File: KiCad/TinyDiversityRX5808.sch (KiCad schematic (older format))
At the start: 23 parts, among them J1 Googles, J2 RX_A, J3 RX_B, J4 Conn_01x06, SW1 SW_Push, U1 MAX4624, U2 ATTINY85-20SU

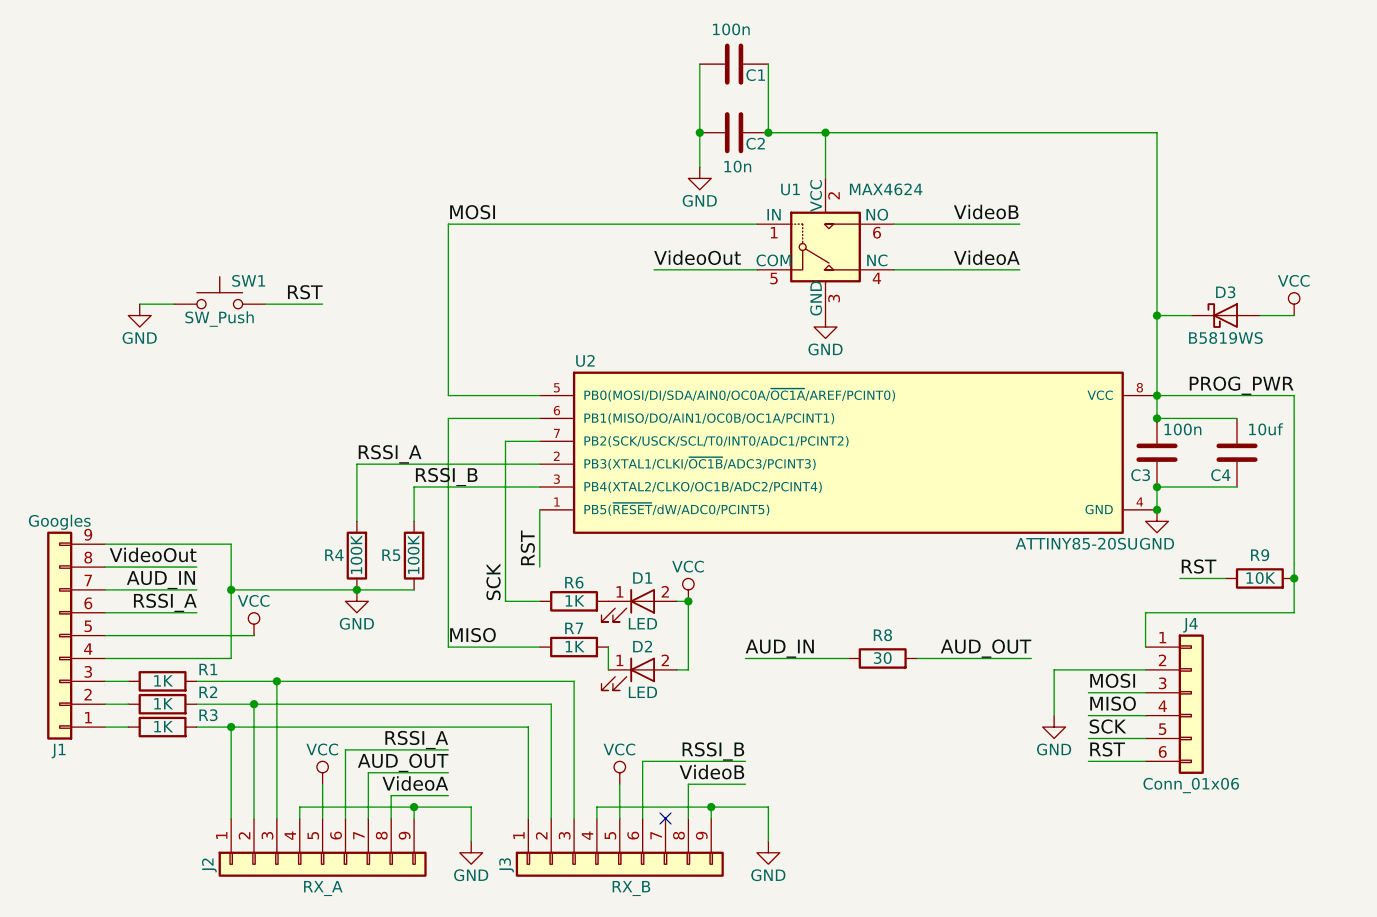
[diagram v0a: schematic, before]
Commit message: Layout change for easier solder and more thin design
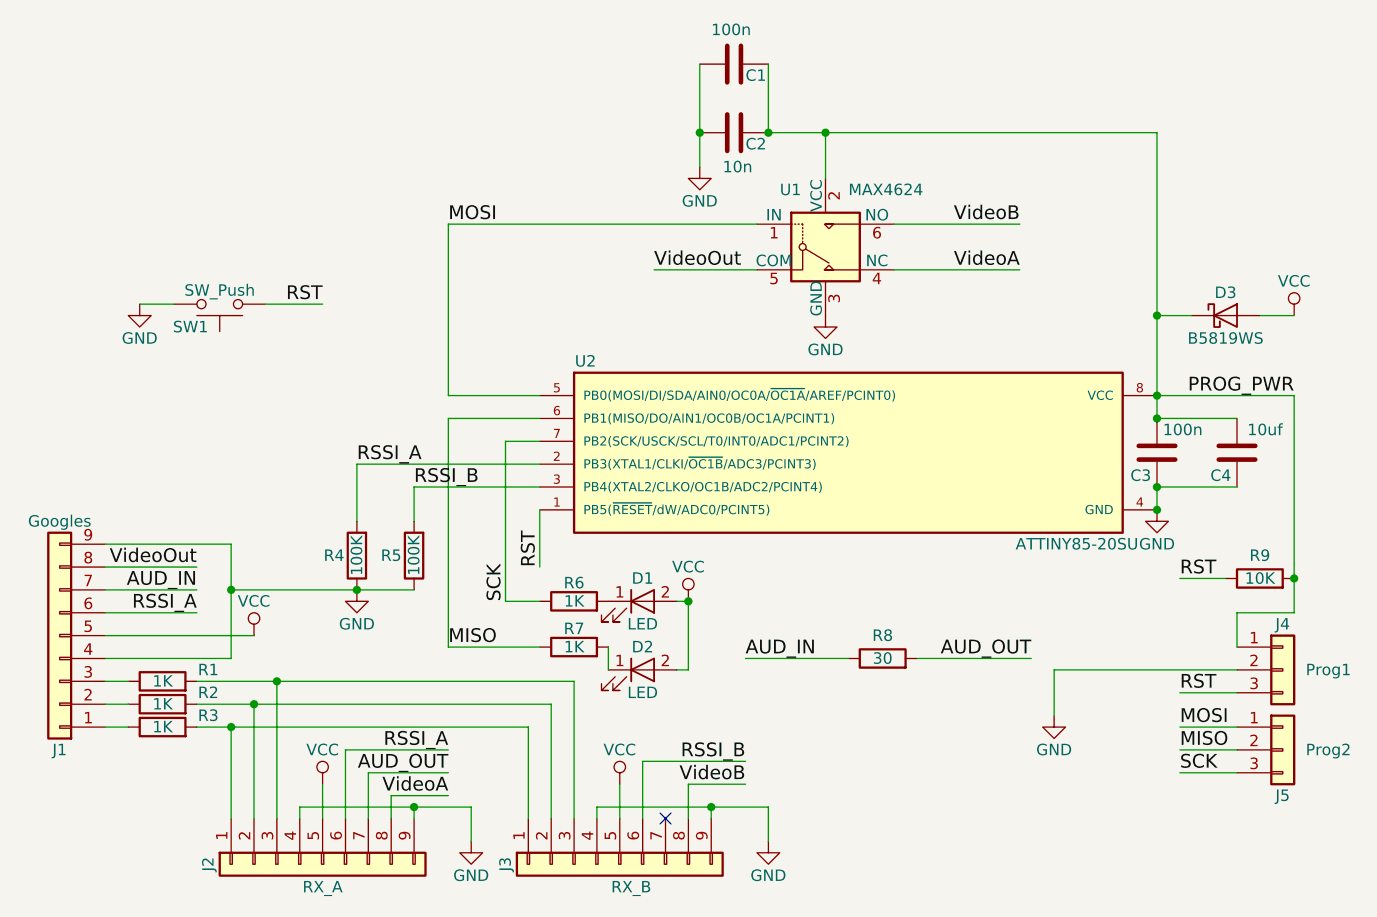
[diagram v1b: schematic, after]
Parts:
- removed J4: Conn_01x06, KiCadCustomLibs:Pads_prog_6pin1.25mm, symbol Conn_01x06
- added J4: Prog1, KiCadCustomLibs:Pads_prog_3pin1.25mm, symbol Conn_01x03
- added J5: Prog2, KiCadCustomLibs:Pads_prog_3pin1.25mm, symbol Conn_01x03
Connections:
- net GND: now also SW1.2, J4.2 (Pin_2); no longer SW1.1
- net MISO: now also J5.2 (Pin_2)
- net MOSI: now also J5.1 (Pin_1)
- net PROG_PWR: now also J4.1 (Pin_1)
- net RST: now also SW1.1, J4.3 (Pin_3); no longer SW1.2
- net SCK: now also J5.3 (Pin_3)
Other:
- moved on the sheet: SW1
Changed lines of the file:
@@
 $EndComp
 $Comp
-L GND #PWR01
+L GND #PWR10
 U 1 1 5A0C59A7
 P 5550 2850
-F 0 "#PWR01" H 5550 2600 50  0001 C CNN
+F 0 "#PWR10" H 5550 2600 50  0001 C CNN
 F 1 "GND" H 5550 2700 50  0000 C CNN
 F 2 "" H 5550 2850 50  0001 C CNN
@@
 $EndComp
 $Comp
-L GND #PWR02
+L GND #PWR12
 U 1 1 5A0C59D1
 P 7000 3700
-F 0 "#PWR02" H 7000 3450 50  0001 C CNN
+F 0 "#PWR12" H 7000 3450 50  0001 C CNN
 F 1 "GND" H 7000 3550 50  0000 C CNN
 F 2 "" H 7000 3700 50  0001 C CNN
@@
 RSSI_B
 $Comp
-L GND #PWR03
+L GND #PWR1
 U 1 1 5A0C5ED9
 P 2550 2800
-F 0 "#PWR03" H 2550 2550 50  0001 C CNN
+F 0 "#PWR1" H 2550 2550 50  0001 C CNN
 F 1 "GND" H 2550 2650 50  0000 C CNN
 F 2 "" H 2550 2800 50  0001 C CNN
@@
 $EndComp
 $Comp
-L VCC #PWR04
+L VCC #PWR13
 U 1 1 5A0C6148
 P 7600 2850
-F 0 "#PWR04" H 7600 2700 50  0001 C CNN
+F 0 "#PWR13" H 7600 2700 50  0001 C CNN
 F 1 "VCC" H 7600 3000 50  0000 C CNN
 F 2 "" H 7600 2850 50  0001 C CNN
@@
 $EndComp
 $Comp
-L VCC #PWR05
+L VCC #PWR2
 U 1 1 5A0C6355
 P 3050 4250
-F 0 "#PWR05" H 3050 4100 50  0001 C CNN
+F 0 "#PWR2" H 3050 4100 50  0001 C CNN
 F 1 "VCC" H 3050 4400 50  0000 C CNN
 F 2 "" H 3050 4250 50  0001 C CNN
@@
 $EndComp
 $Comp
-L GND #PWR06
+L GND #PWR8
 U 1 1 5A0C6978
 P 5000 2200
-F 0 "#PWR06" H 5000 1950 50  0001 C CNN
+F 0 "#PWR8" H 5000 1950 50  0001 C CNN
 F 1 "GND" H 5000 2050 50  0000 C CNN
 F 2 "" H 5000 2200 50  0001 C CNN
@@
 $EndComp
 $Comp
-L VCC #PWR07
+L VCC #PWR7
 U 1 1 5A0C6F3D
 P 4950 4100
-F 0 "#PWR07" H 4950 3950 50  0001 C CNN
+F 0 "#PWR7" H 4950 3950 50  0001 C CNN
 F 1 "VCC" H 4950 4250 50  0000 C CNN
 F 2 "" H 4950 4100 50  0001 C CNN
@@
 $EndComp
 $Comp
-L GND #PWR08
+L GND #PWR4
 U 1 1 5A0C7B39
 P 3500 4050
-F 0 "#PWR08" H 3500 3800 50  0001 C CNN
+F 0 "#PWR4" H 3500 3800 50  0001 C CNN
 F 1 "GND" H 3500 3900 50  0000 C CNN
 F 2 "" H 3500 4050 50  0001 C CNN
@@
 $EndComp
 $Comp
-L GND #PWR09
+L GND #PWR5
 U 1 1 5A0C82E6
 P 4000 5150
-F 0 "#PWR09" H 4000 4900 50  0001 C CNN
+F 0 "#PWR5" H 4000 4900 50  0001 C CNN
 F 1 "GND" H 4000 5000 50  0000 C CNN
 F 2 "" H 4000 5150 50  0001 C CNN
@@
 $EndComp
 $Comp
-L GND #PWR010
+L GND #PWR9
 U 1 1 5A0C83DD
 P 5300 5150
-F 0 "#PWR010" H 5300 4900 50  0001 C CNN
+F 0 "#PWR9" H 5300 4900 50  0001 C CNN
 F 1 "GND" H 5300 5000 50  0000 C CNN
 F 2 "" H 5300 5150 50  0001 C CNN
@@
 $EndComp
 $Comp
-L VCC #PWR011
+L VCC #PWR3
 U 1 1 5A0C85A9
 P 3350 4900
-F 0 "#PWR011" H 3350 4750 50  0001 C CNN
+F 0 "#PWR3" H 3350 4750 50  0001 C CNN
 F 1 "VCC" H 3350 5050 50  0000 C CNN
 F 2 "" H 3350 4900 50  0001 C CNN
@@
 $EndComp
 $Comp
-L VCC #PWR012
+L VCC #PWR6
 U 1 1 5A0C85E1
 P 4650 4900
-F 0 "#PWR012" H 4650 4750 50  0001 C CNN
+F 0 "#PWR6" H 4650 4750 50  0001 C CNN
 F 1 "VCC" H 4650 5050 50  0000 C CNN
 F 2 "" H 4650 4900 50  0001 C CNN
@@
 Text Label 3900 2450 0    60   ~ 0
 MOSI
-Text Label 6700 4500 0    60   ~ 0
+Text Label 7100 4650 0    60   ~ 0
 MOSI
 Wire Wire Line
@@
 Text Label 4300 3950 1    60   ~ 0
 RST
-Wire Wire Line
-	6950 4600 6700 4600
-Text Label 6700 4800 0    60   ~ 0
+Text Label 7100 4500 0    60   ~ 0
 RST
-Wire Wire Line
-	6950 4700 6700 4700
-Text Label 6700 4700 0    60   ~ 0
+Text Label 7100 4850 0    60   ~ 0
 SCK
-Wire Wire Line
-	6950 4800 6700 4800
-Text Label 6700 4600 0    60   ~ 0
+Text Label 7100 4750 0    60   ~ 0
 MISO
 Wire Wire Line
@@
 	3900 2450 5250 2450
 $Comp
-L Conn_01x06 J4
-U 1 1 5A3920B9
-P 7150 4500
-F 0 "J4" H 7150 4800 50  0000 C CNN
-F 1 "Conn_01x06" H 7150 4100 50  0000 C CNN
-F 2 "KiCadCustomLibs:Pads_prog_6pin1.25mm" H 7150 4500 50  0001 C CNN
-F 3 "" H 7150 4500 50  0001 C CNN
-	1    7150 4500
-	1    0    0    -1
-$EndComp
-Wire Wire Line
-	7600 4150 6950 4150
-Wire Wire Line
-	6950 4150 6950 4300
-$Comp
-L GND #PWR013
+L GND #PWR11
 U 1 1 5A392520
 P 6550 4600
-F 0 "#PWR013" H 6550 4350 50  0001 C CNN
+F 0 "#PWR11" H 6550 4350 50  0001 C CNN
 F 1 "GND" H 6550 4450 50  0000 C CNN
 F 2 "" H 6550 4600 50  0001 C CNN
@@
 F 3 "" H 2900 3000 50  0001 C CNN
 	1    2900 2800
-	1    0    0    -1
+	-1   0    0    1
 $EndComp
 $Comp
@@
 $EndComp
 Wire Wire Line
-	6950 4500 6700 4500
-Wire Wire Line
 	6550 4600 6550 4400
 Wire Wire Line
-	6550 4400 6950 4400
+	6550 4400 7350 4400
+$Comp
+L Conn_01x03 J4
+U 1 1 5B27CDDD
+P 7550 4400
+F 0 "J4" H 7550 4600 50  0000 C CNN
+F 1 "Prog1" H 7750 4400 50  0000 C CNN
+F 2 "KiCadCustomLibs:Pads_prog_3pin1.25mm" H 7550 4400 50  0001 C CNN
+F 3 "" H 7550 4400 50  0001 C CNN
+	1    7550 4400
+	1    0    0    -1
+$EndComp
+$Comp
+L Conn_01x03 J5
+U 1 1 5B27CE42
+P 7550 4750
+F 0 "J5" H 7550 4550 50  0000 C CNN
+F 1 "Prog2" H 7750 4750 50  0000 C CNN
+F 2 "KiCadCustomLibs:Pads_prog_3pin1.25mm" H 7550 4750 50  0001 C CNN
+F 3 "" H 7550 4750 50  0001 C CNN
+	1    7550 4750
+	1    0    0    -1
+$EndComp
+Wire Wire Line
+	7600 4150 7350 4150
+Wire Wire Line
+	7350 4150 7350 4300
+Wire Wire Line
+	7350 4500 7100 4500
+Wire Wire Line
+	7350 4650 7100 4650
+Wire Wire Line
+	7350 4750 7100 4750
+Wire Wire Line
+	7350 4850 7100 4850
 $EndSCHEMATC
